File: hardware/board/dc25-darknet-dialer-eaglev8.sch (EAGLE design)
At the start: 81 parts, among them SW1 RESET, X1 10118193-0001LF, Y1 RESONATORSMD

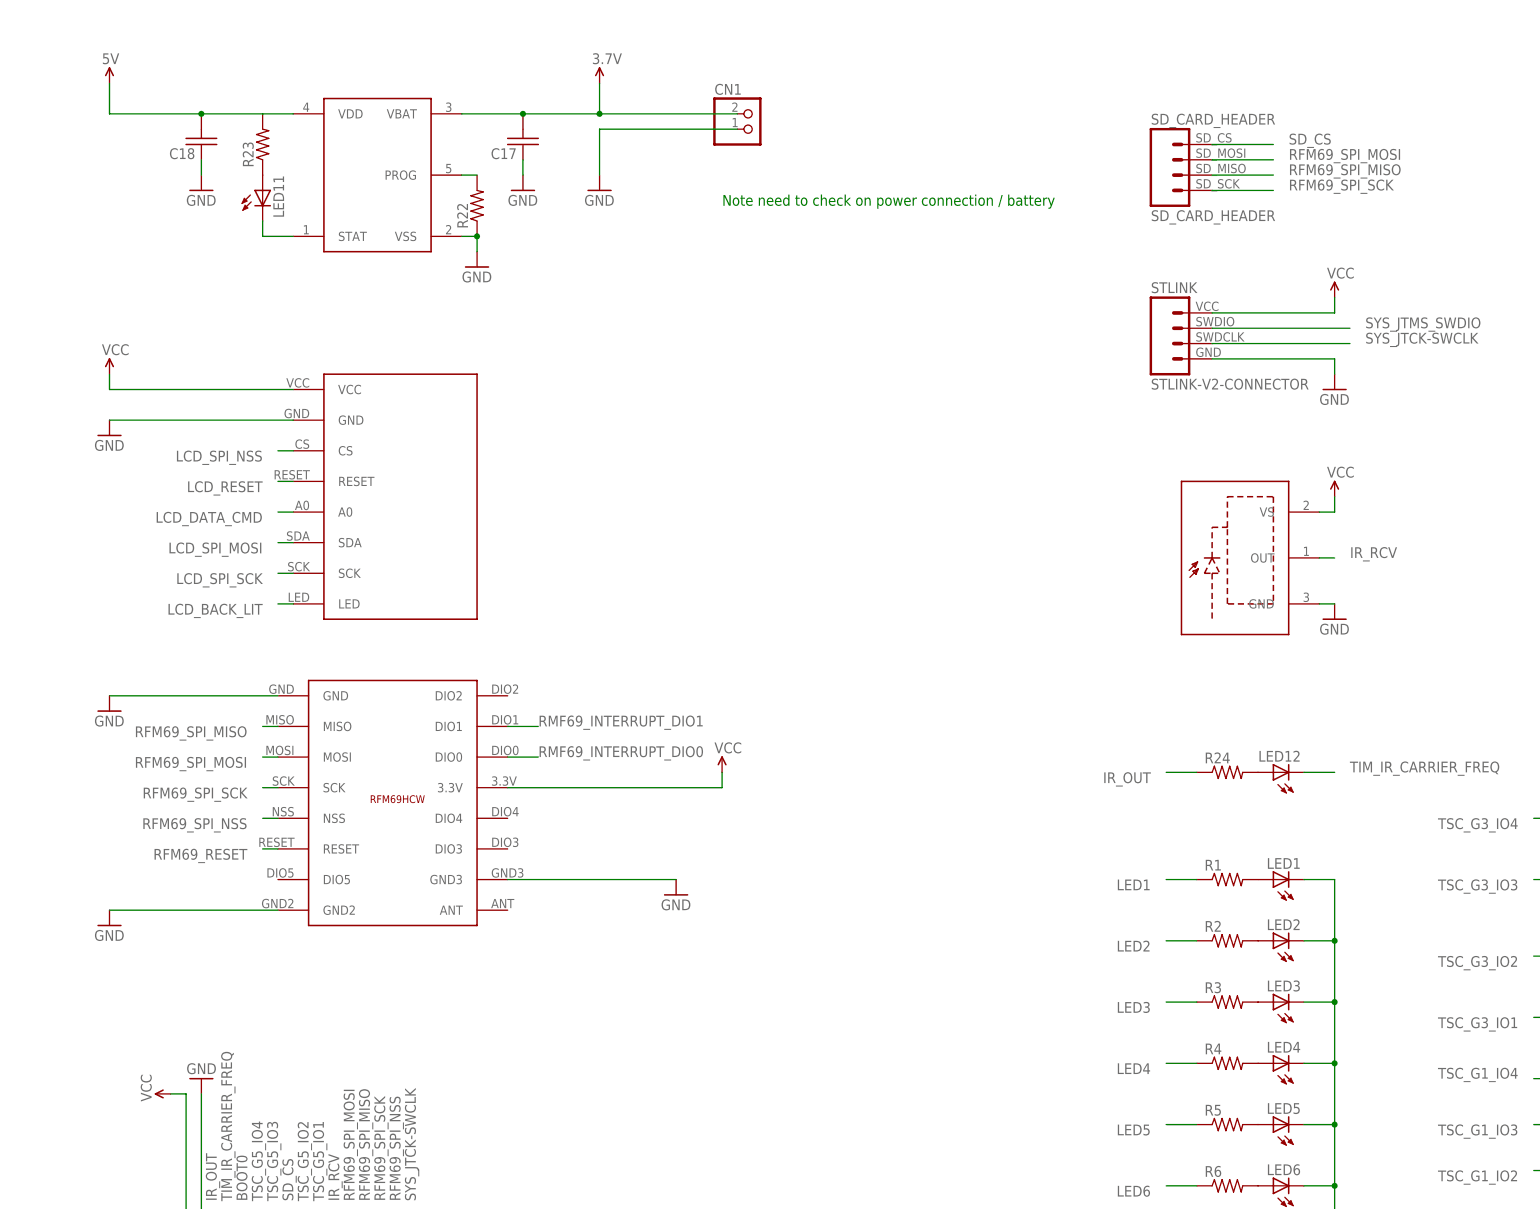
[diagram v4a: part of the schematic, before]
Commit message: Updated display module, added antenna design
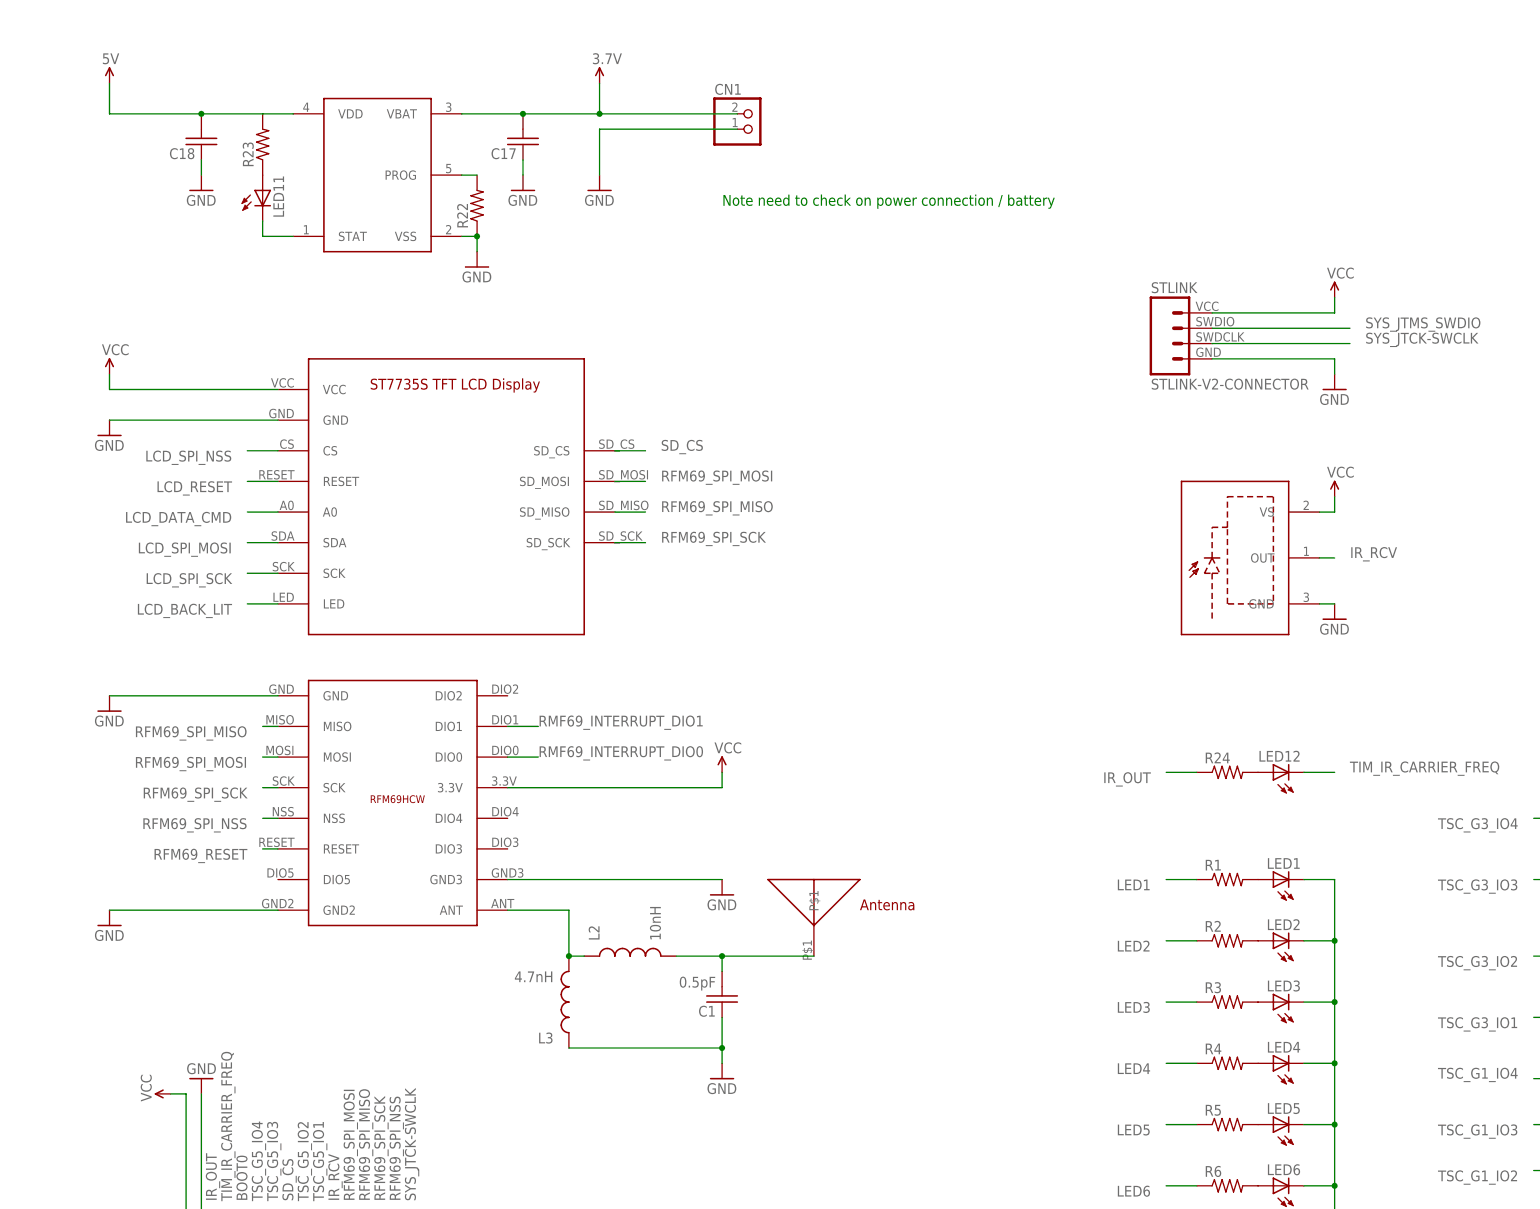
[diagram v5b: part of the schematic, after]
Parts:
- removed SD_CARD_HEADER: SD_CARD_HEADER, darknet_parts_library:SD_CARD_HEADER
- removed U$12: COLOR_LCD_MODULE, darknet_parts_library:COLOR_LCD_MODULE
- added C1: 0.5pF, darknet_parts_library:C-USC0603
- added L2: 10nH, darknet_parts_library:INDUCTOR0603
- added L3: 4.7nH, darknet_parts_library:INDUCTOR0603
- added U$21: CHIP_ANTENNA, darknet_parts_library:CHIP_ANTENNA
- added U$22: ST7735S_LCD_MODULE, darknet_parts_library:ST7735S_LCD_MODULE
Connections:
- new net ANT: L2.1, L3.2, U$15.ANT
- new net N$31: C1.2, L2.2, U$21.P$1
- net GND: now also C1.1, L3.1, U$22.GND; no longer U$12.GND
- net LCD_BACK_LIT: now also U$22.LED; no longer U$12.LED
- net LCD_DATA_CMD: now also U$22.A0; no longer U$12.A0
- net LCD_RESET: now also U$22.RESET; no longer U$12.RESET
- net LCD_SPI_MOSI: now also U$22.SDA; no longer U$12.SDA
- net LCD_SPI_NSS: now also U$22.CS; no longer U$12.CS
- net LCD_SPI_SCK: now also U$22.SCK; no longer U$12.SCK
- net RFM69_SPI_MISO: now also U$22.SD_MISO; no longer SD_CARD_HEADER.SD_MISO
- net RFM69_SPI_MOSI: now also U$22.SD_MOSI; no longer SD_CARD_HEADER.SD_MOSI
- net RFM69_SPI_SCK: now also U$22.SD_SCK; no longer SD_CARD_HEADER.SD_SCK
- net SD_CS: now also U$22.SD_CS; no longer SD_CARD_HEADER.SD_CS
- net VCC: now also U$22.VCC; no longer U$12.VCC
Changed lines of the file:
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@@
 <part name="TOUCH9" library="darknet_parts_library" deviceset="CAP_TOUCH" device="9" value="CAP_TOUCH9"/>
 <part name="TOUCH0" library="darknet_parts_library" deviceset="CAP_TOUCH" device="0" value="CAP_TOUCH0"/>
-<part name="U$12" library="darknet_parts_library" deviceset="COLOR_LCD_MODULE" device=""/>
 <part name="LED1" library="SYNShop" deviceset="LED" device="REVERSEMOUNT"/>
 <part name="LED2" library="SYNShop" deviceset="LED" device="REVERSEMOUNT"/>
@@
 <part name="SAMPLE_CAP_G2" library="darknet_parts_library" deviceset="C-US" device="C0603" value="0.047uF"/>
 <part name="SAMPLE_CAP_G5" library="darknet_parts_library" deviceset="C-US" device="C0603" value="0.047uF"/>
-<part name="SD_CARD_HEADER" library="darknet_parts_library" deviceset="SD_CARD_HEADER" device=""/>
 <part name="GND1" library="SYNShop" deviceset="GND" device=""/>
 <part name="GND11" library="SYNShop" deviceset="GND" device=""/>
@@
 <part name="U$19" library="darknet_parts_library" deviceset="TLV702" device=""/>
 <part name="GND15" library="SYNShop" deviceset="GND" device=""/>
+<part name="U$21" library="darknet_parts_library" deviceset="CHIP_ANTENNA" device=""/>
+<part name="C1" library="darknet_parts_library" deviceset="C-US" device="C0603" value="0.5pF"/>
+<part name="GND16" library="SYNShop" deviceset="GND" device=""/>
+<part name="L2" library="darknet_parts_library" deviceset="INDUCTOR" device="0603" value="10nH"/>
+<part name="L3" library="darknet_parts_library" deviceset="INDUCTOR" device="0603" value="4.7nH"/>
+<part name="U$22" library="darknet_parts_library" deviceset="ST7735S_LCD_MODULE" device=""/>
 </parts>
 <sheets>
@@
 <instance part="TOUCH9" gate="G$1" x="317.5" y="78.74"/>
 <instance part="TOUCH0" gate="G$1" x="317.5" y="68.58"/>
-<instance part="U$12" gate="G$1" x="96.52" y="259.08"/>
 <instance part="LED1" gate="G$1" x="254" y="177.8" rot="R90"/>
 <instance part="LED2" gate="G$1" x="254" y="167.64" rot="R90"/>
@@
 <instance part="GND2" gate="1" x="60.96" y="205.74"/>
 <instance part="GND3" gate="1" x="60.96" y="170.18"/>
-<instance part="GND4" gate="1" x="154.94" y="175.26"/>
+<instance part="GND4" gate="1" x="162.56" y="175.26"/>
 <instance part="GND5" gate="1" x="60.96" y="251.46"/>
 <instance part="GND6" gate="1" x="264.16" y="71.12"/>
@@
 <instance part="SAMPLE_CAP_G2" gate="G$1" x="332.74" y="114.3" rot="R90"/>
 <instance part="SAMPLE_CAP_G5" gate="G$1" x="332.74" y="86.36" rot="R90"/>
-<instance part="SD_CARD_HEADER" gate="G$1" x="243.84" y="292.1"/>
 <instance part="GND1" gate="1" x="340.36" y="81.28"/>
 <instance part="GND11" gate="1" x="340.36" y="109.22"/>
@@
 <instance part="U$19" gate="G$1" x="101.6" y="391.16"/>
 <instance part="GND15" gate="1" x="101.6" y="373.38"/>
+<instance part="U$21" gate="G$1" x="177.8" y="170.18"/>
+<instance part="C1" gate="G$1" x="162.56" y="157.48" rot="R180"/>
+<instance part="GND16" gate="1" x="162.56" y="144.78"/>
+<instance part="L2" gate="G$1" x="147.32" y="165.1" rot="R90"/>
+<instance part="L3" gate="G$1" x="137.16" y="157.48" rot="R180"/>
+<instance part="U$22" gate="G$1" x="116.84" y="241.3"/>
 </instances>
 <busses>
@@
 <pinref part="U$15" gate="G$1" pin="GND3"/>
 <pinref part="GND4" gate="1" pin="GND"/>
-<wire x1="127" y1="177.8" x2="154.94" y2="177.8" width="0.1524" layer="91"/>
-</segment>
-<segment>
-<pinref part="U$12" gate="G$1" pin="GND"/>
+<wire x1="127" y1="177.8" x2="162.56" y2="177.8" width="0.1524" layer="91"/>
+</segment>
+<segment>
 <pinref part="GND5" gate="1" pin="GND"/>
-<wire x1="91.44" y1="254" x2="60.96" y2="254" width="0.1524" layer="91"/>
+<wire x1="88.9" y1="254" x2="60.96" y2="254" width="0.1524" layer="91"/>
+<pinref part="U$22" gate="G$1" pin="GND"/>
 </segment>
 <segment>
@@
 <junction x="101.6" y="378.46"/>
 </segment>
+<segment>
+<pinref part="C1" gate="G$1" pin="1"/>
+<pinref part="GND16" gate="1" pin="GND"/>
+<wire x1="162.56" y1="154.94" x2="162.56" y2="149.86" width="0.1524" layer="91"/>
+<pinref part="L3" gate="G$1" pin="1"/>
+<wire x1="162.56" y1="149.86" x2="162.56" y2="147.32" width="0.1524" layer="91"/>
+<wire x1="137.16" y1="149.86" x2="162.56" y2="149.86" width="0.1524" layer="91"/>
+<junction x="162.56" y="149.86"/>
+</segment>
 </net>
 <net name="N$12" class="0">
@@
 </segment>
 <segment>
-<pinref part="SD_CARD_HEADER" gate="G$1" pin="SD_MISO"/>
-<wire x1="243.84" y1="294.64" x2="254" y2="294.64" width="0.1524" layer="91"/>
-<label x="256.54" y="294.64" size="1.778" layer="95"/>
+<wire x1="144.78" y1="238.76" x2="149.86" y2="238.76" width="0.1524" layer="91"/>
+<label x="152.4" y="238.76" size="1.778" layer="95"/>
+<pinref part="U$22" gate="G$1" pin="SD_MISO"/>
 </segment>
 </net>
@@
 </segment>
 <segment>
-<pinref part="SD_CARD_HEADER" gate="G$1" pin="SD_MOSI"/>
-<wire x1="243.84" y1="297.18" x2="254" y2="297.18" width="0.1524" layer="91"/>
-<label x="256.54" y="297.18" size="1.778" layer="95"/>
+<wire x1="144.78" y1="243.84" x2="149.86" y2="243.84" width="0.1524" layer="91"/>
+<label x="152.4" y="243.84" size="1.778" layer="95"/>
+<pinref part="U$22" gate="G$1" pin="SD_MOSI"/>
 </segment>
 </net>
@@
 </segment>
 <segment>
-<pinref part="SD_CARD_HEADER" gate="G$1" pin="SD_SCK"/>
-<wire x1="243.84" y1="292.1" x2="254" y2="292.1" width="0.1524" layer="91"/>
-<label x="256.54" y="292.1" size="1.778" layer="95"/>
+<wire x1="144.78" y1="233.68" x2="149.86" y2="233.68" width="0.1524" layer="91"/>
+<label x="152.4" y="233.68" size="1.778" layer="95"/>
+<pinref part="U$22" gate="G$1" pin="SD_SCK"/>
 </segment>
 </net>
@@
 </segment>
 <segment>
-<pinref part="U$12" gate="G$1" pin="CS"/>
-<wire x1="91.44" y1="248.92" x2="88.9" y2="248.92" width="0.1524" layer="91"/>
-<label x="86.36" y="248.92" size="1.778" layer="95" rot="R180"/>
+<wire x1="88.9" y1="248.92" x2="83.82" y2="248.92" width="0.1524" layer="91"/>
+<label x="81.28" y="248.92" size="1.778" layer="95" rot="R180"/>
+<pinref part="U$22" gate="G$1" pin="CS"/>
 </segment>
 </net>
@@
 </segment>
 <segment>
-<pinref part="U$12" gate="G$1" pin="VCC"/>
 <pinref part="U$9" gate="G$1" pin="VCC"/>
-<wire x1="91.44" y1="259.08" x2="60.96" y2="259.08" width="0.1524" layer="91"/>
+<wire x1="88.9" y1="259.08" x2="60.96" y2="259.08" width="0.1524" layer="91"/>
 <wire x1="60.96" y1="259.08" x2="60.96" y2="261.62" width="0.1524" layer="91"/>
+<pinref part="U$22" gate="G$1" pin="VCC"/>
 </segment>
 <segment>
@@
 </segment>
 <segment>
-<pinref part="SD_CARD_HEADER" gate="G$1" pin="SD_CS"/>
-<wire x1="243.84" y1="299.72" x2="254" y2="299.72" width="0.1524" layer="91"/>
-<label x="256.54" y="299.72" size="1.778" layer="95"/>
+<wire x1="144.78" y1="248.92" x2="149.86" y2="248.92" width="0.1524" layer="91"/>
+<label x="152.4" y="248.92" size="1.778" layer="95"/>
+<pinref part="U$22" gate="G$1" pin="SD_CS"/>
 </segment>
 </net>
@@
 </segment>
 <segment>
-<pinref part="U$12" gate="G$1" pin="RESET"/>
-<wire x1="91.44" y1="243.84" x2="88.9" y2="243.84" width="0.1524" layer="91"/>
-<label x="86.36" y="243.84" size="1.778" layer="95" rot="R180"/>
+<wire x1="88.9" y1="243.84" x2="83.82" y2="243.84" width="0.1524" layer="91"/>
+<label x="81.28" y="243.84" size="1.778" layer="95" rot="R180"/>
+<pinref part="U$22" gate="G$1" pin="RESET"/>
 </segment>
 </net>
@@
 </segment>
 <segment>
-<pinref part="U$12" gate="G$1" pin="LED"/>
-<wire x1="91.44" y1="223.52" x2="88.9" y2="223.52" width="0.1524" layer="91"/>
-<label x="86.36" y="223.52" size="1.778" layer="95" rot="R180"/>
+<wire x1="88.9" y1="223.52" x2="83.82" y2="223.52" width="0.1524" layer="91"/>
+<label x="81.28" y="223.52" size="1.778" layer="95" rot="R180"/>
+<pinref part="U$22" gate="G$1" pin="LED"/>
 </segment>
 </net>
@@
 </segment>
 <segment>
-<pinref part="U$12" gate="G$1" pin="SDA"/>
-<wire x1="91.44" y1="233.68" x2="88.9" y2="233.68" width="0.1524" layer="91"/>
-<label x="86.36" y="233.68" size="1.778" layer="95" rot="R180"/>
+<wire x1="88.9" y1="233.68" x2="83.82" y2="233.68" width="0.1524" layer="91"/>
+<label x="81.28" y="233.68" size="1.778" layer="95" rot="R180"/>
+<pinref part="U$22" gate="G$1" pin="SDA"/>
 </segment>
 </net>
@@
 </segment>
 <segment>
-<pinref part="U$12" gate="G$1" pin="A0"/>
-<wire x1="91.44" y1="238.76" x2="88.9" y2="238.76" width="0.1524" layer="91"/>
-<label x="86.36" y="238.76" size="1.778" layer="95" rot="R180"/>
+<wire x1="88.9" y1="238.76" x2="83.82" y2="238.76" width="0.1524" layer="91"/>
+<label x="81.28" y="238.76" size="1.778" layer="95" rot="R180"/>
+<pinref part="U$22" gate="G$1" pin="A0"/>
 </segment>
 </net>
@@
 </segment>
 <segment>
-<pinref part="U$12" gate="G$1" pin="SCK"/>
-<wire x1="91.44" y1="228.6" x2="88.9" y2="228.6" width="0.1524" layer="91"/>
-<label x="86.36" y="228.6" size="1.778" layer="95" rot="R180"/>
+<wire x1="88.9" y1="228.6" x2="83.82" y2="228.6" width="0.1524" layer="91"/>
+<label x="81.28" y="228.6" size="1.778" layer="95" rot="R180"/>
+<pinref part="U$22" gate="G$1" pin="SCK"/>
 </segment>
 </net>
@@
 </segment>
 </net>
+<net name="ANT" class="0">
+<segment>
+<pinref part="U$15" gate="G$1" pin="ANT"/>
+<wire x1="127" y1="172.72" x2="137.16" y2="172.72" width="0.1524" layer="91"/>
+<pinref part="L2" gate="G$1" pin="1"/>
+<pinref part="L3" gate="G$1" pin="2"/>
+<wire x1="139.7" y1="165.1" x2="137.16" y2="165.1" width="0.1524" layer="91"/>
+<wire x1="137.16" y1="172.72" x2="137.16" y2="165.1" width="0.1524" layer="91"/>
+<junction x="137.16" y="165.1"/>
+</segment>
+</net>
+<net name="N$31" class="0">
+<segment>
+<pinref part="L2" gate="G$1" pin="2"/>
+<wire x1="154.94" y1="165.1" x2="162.56" y2="165.1" width="0.1524" layer="91"/>
+<pinref part="C1" gate="G$1" pin="2"/>
+<wire x1="162.56" y1="165.1" x2="162.56" y2="162.56" width="0.1524" layer="91"/>
+<pinref part="U$21" gate="G$1" pin="P$1"/>
+<wire x1="162.56" y1="165.1" x2="177.8" y2="165.1" width="0.1524" layer="91"/>
+<junction x="162.56" y="165.1"/>
+</segment>
+</net>
